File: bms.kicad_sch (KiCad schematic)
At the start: 4 parts, among them U1 BQ76972PFBR

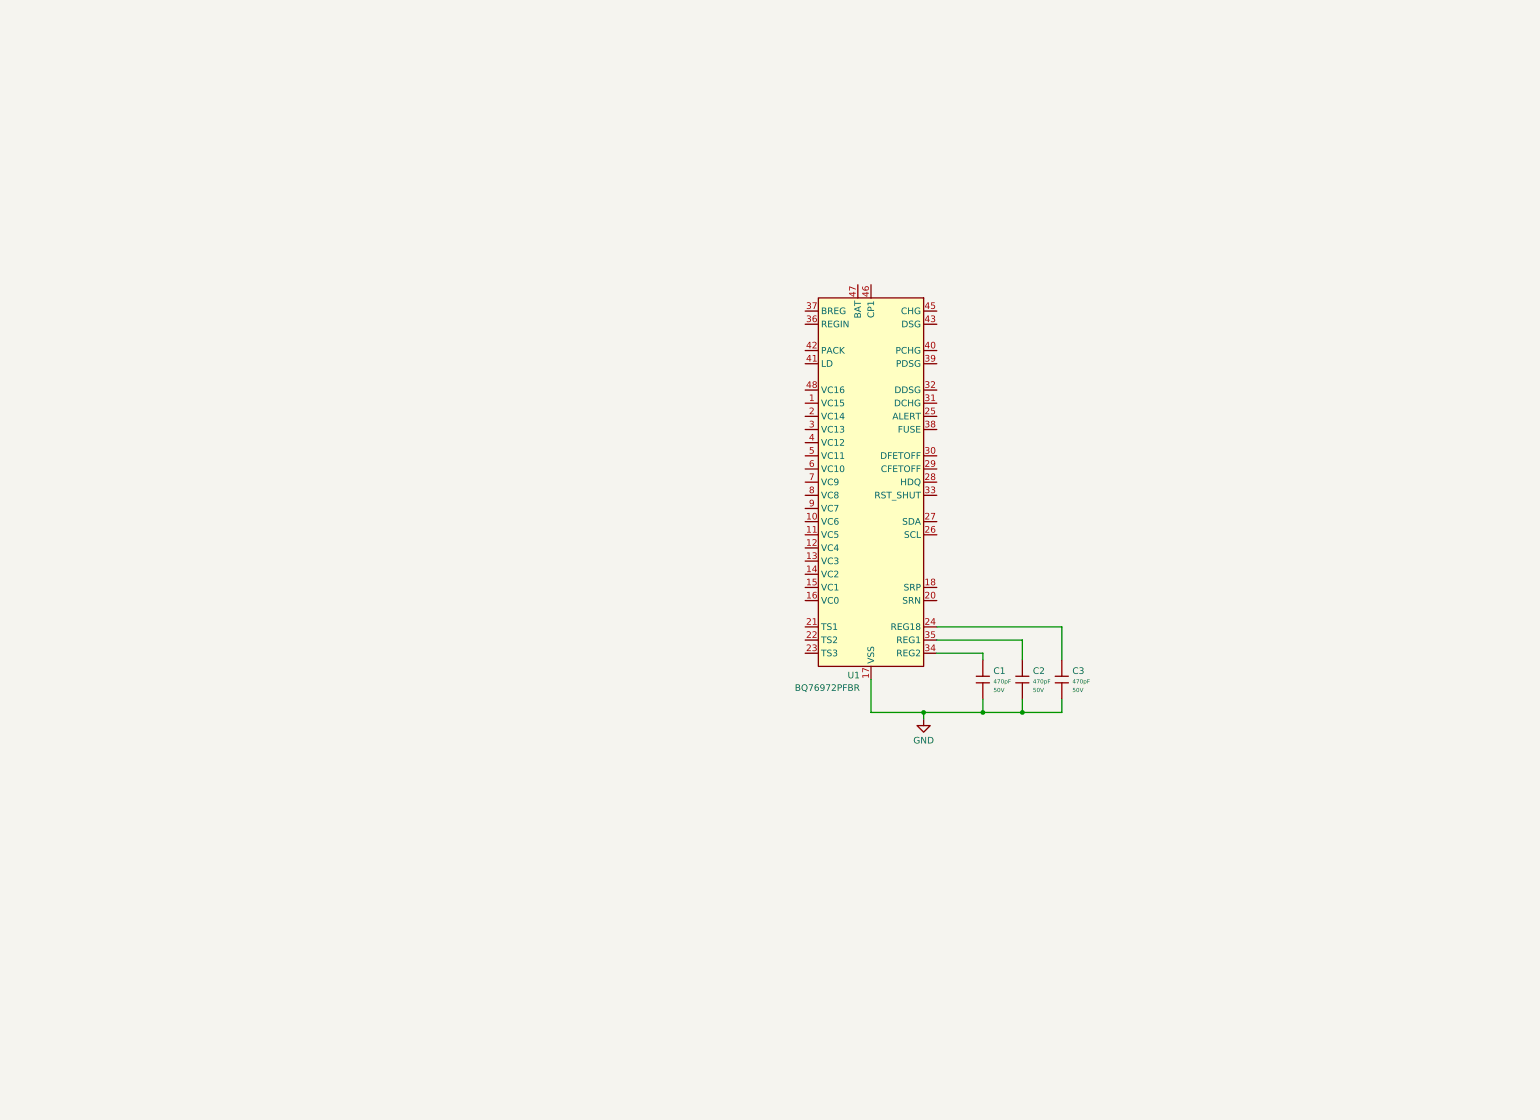
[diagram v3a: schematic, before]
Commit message: removed regulator circuit, more mosfet testing with ltspice
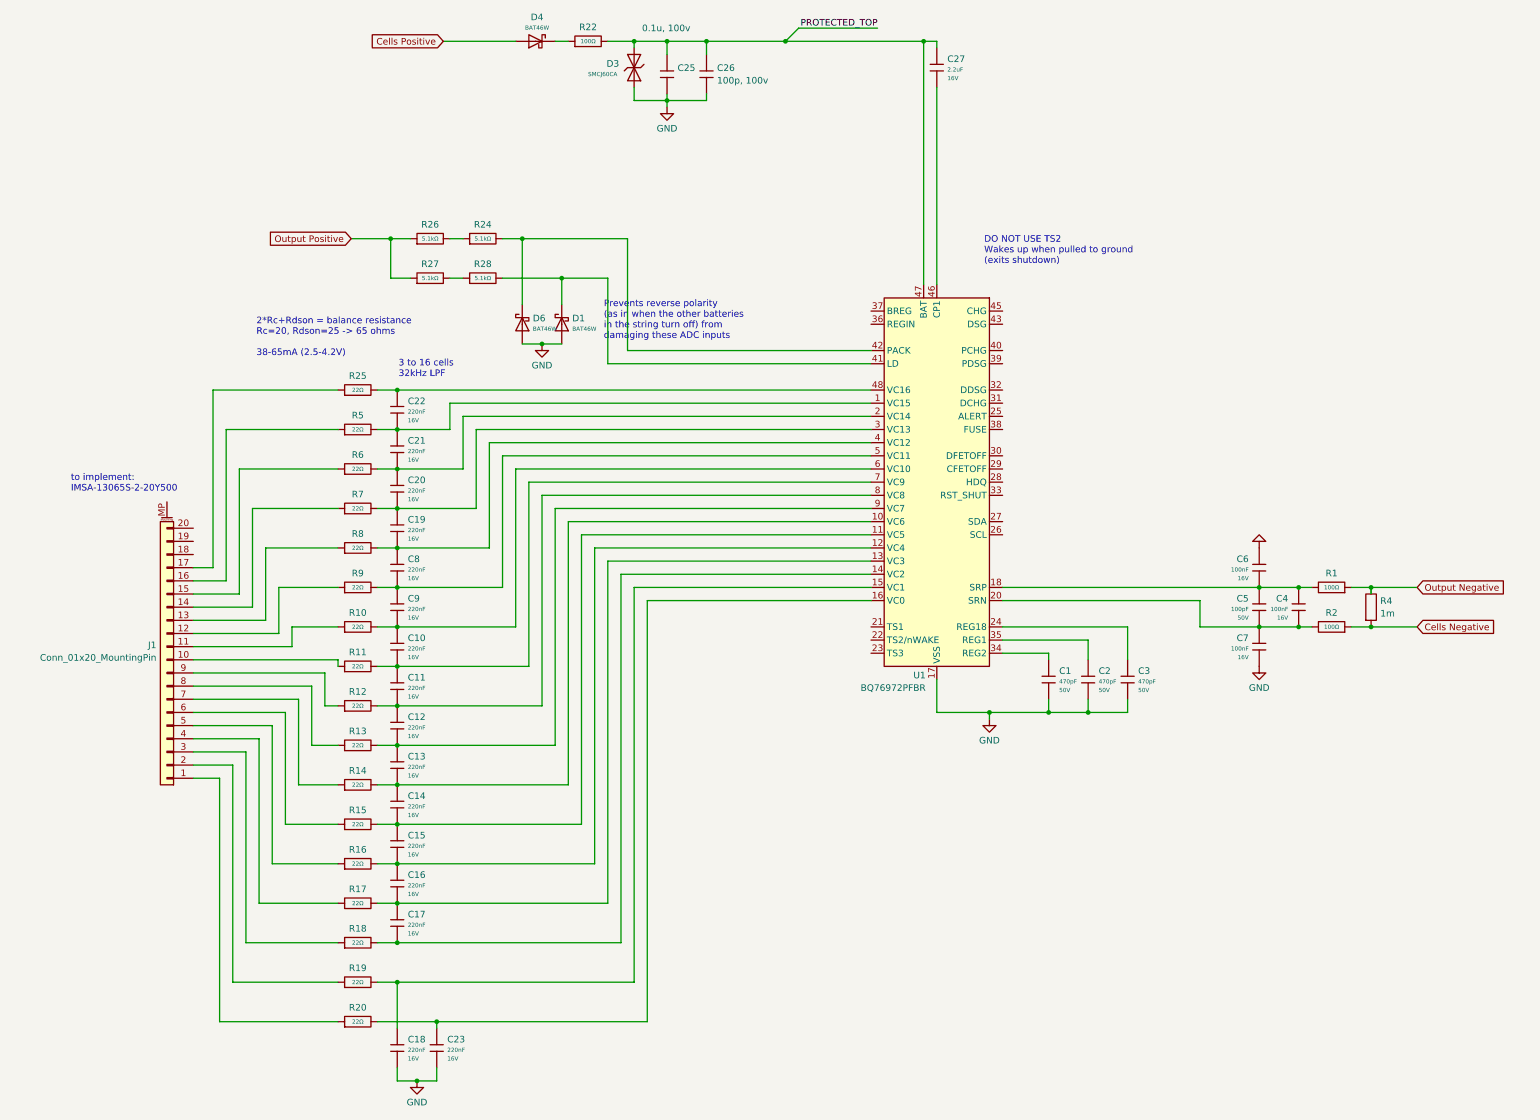
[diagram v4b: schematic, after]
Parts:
- added C10, C11, C12, C13, C14, C15, C16, C17, C18, C19, C20, C21, C22, C23, C8, C9: 220nF, PCM_JLCPCB:C_0402, symbol PCM_JLCPCB-Capacitors:0402,220nF
- added C25: 0.1u, 100v, symbol ct_lib:C
- added C26: 100p, 100v, symbol ct_lib:C
- added C27: 2.2uF, PCM_JLCPCB:C_0603, symbol PCM_JLCPCB-Capacitors:0603,2.2uF
- added C4, C6, C7: 100nF, PCM_JLCPCB:C_0402, symbol PCM_JLCPCB-Capacitors:0402,100nF
- added C5: 100pF, PCM_JLCPCB:C_0402, symbol PCM_JLCPCB-Capacitors:0402,100pF
- added D1, D4, D6: BAT46W, PCM_JLCPCB:D_SOD-123, symbol PCM_JLCPCB-Diodes:Schottky,BAT46W
- added D3: SMCJ60CA, PCM_JLCPCB:D_SMC, symbol PCM_JLCPCB-Diodes:TVS-Bi,SMCJ60CA
- added J1: Conn_01x20_MountingPin, symbol Connector_Generic_MountingPin:Conn_01x20_MountingPin
- added R1, R2, R22: 100Ω, PCM_JLCPCB:R_0402, symbol PCM_JLCPCB-Resistors:0402,100Ω
- added R10, R11, R12, R13, R14, R15, R16, R17, R18, R19, R20, R25, R5, R6, R7, R8, R9: 22Ω, PCM_JLCPCB:R_0402, symbol PCM_JLCPCB-Resistors:0402,22Ω
- added R24, R26, R27, R28: 5.1kΩ, PCM_JLCPCB:R_0402, symbol PCM_JLCPCB-Resistors:0402,5.1kΩ
- added R4: 1m, symbol ct_lib:R
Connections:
- net GND: now also C18.2, C23.2, C25.2, C26.2, C6.1, C7.2, D1.2, D3.1, D6.2
- net at U1.1 (VC15): now also C21.1, C22.2, R5.2
- net at U1.10 (VC6): now also C13.2, C14.1, R14.2
- net at U1.11 (VC5): now also C14.2, C15.1, R15.2
- net at U1.12 (VC4): now also C15.2, C16.1, R16.2
- net at U1.13 (VC3): now also C16.2, C17.1, R17.2
- net at U1.14 (VC2): now also C17.2, R18.2
- net at U1.15 (VC1): now also C18.1, R19.2
- net at U1.16 (VC0): now also C23.1, R20.2
- net at U1.18 (SRP): now also C4.1, C5.1, C6.2, R1.2
- net at U1.2 (VC14): now also C20.1, C21.2, R6.2
- net at U1.20 (SRN): now also C4.2, C5.2, C7.1, R2.2
- net at U1.3 (VC13): now also C19.1, C20.2, R7.2
- net at U1.4 (VC12): now also C19.2, C8.1, R8.2
- net at U1.41 (LD): now also D1.1, R28.2
- net at U1.42 (PACK): now also D6.1, R24.2
- net at U1.46 (CP1): now also C27.2
- net at U1.47 (BAT): now also C25.1, C26.1, C27.1, D3.2, R22.2
- net at U1.48 (VC16): now also C22.1, R25.2
- net at U1.5 (VC11): now also C8.2, C9.1, R9.2
- net at U1.6 (VC10): now also C10.1, C9.2, R10.2
- net at U1.7 (VC9): now also C10.2, C11.1, R11.2
- net at U1.8 (VC8): now also C11.2, C12.1, R12.2
- net at U1.9 (VC7): now also C12.2, C13.1, R13.2
- new net: J1.4 (Pin_4), R17.1
- new net: R27.2, R28.1
- new net: J1.5 (Pin_5), R16.1
- new net: J1.15 (Pin_15), R6.1
- new net: J1.3 (Pin_3), R18.1
- new net: D4.1, R22.1
- new net: J1.17 (Pin_17), R25.1
- new net: J1.14 (Pin_14), R7.1
- new net: J1.12 (Pin_12), R9.1
- new net: R24.1, R26.2
- new net: J1.13 (Pin_13), R8.1
- new net: J1.7 (Pin_7), R14.1
- new net: J1.10 (Pin_10), R11.1
- new net: J1.2 (Pin_2), R19.1
- new net: J1.1 (Pin_1), R20.1
- new net: J1.11 (Pin_11), R10.1
- new net: J1.16 (Pin_16), R5.1
- new net: J1.6 (Pin_6), R15.1
- new net: J1.8 (Pin_8), R13.1
- new net: J1.9 (Pin_9), R12.1
- new net Cells Negative: R2.1, R4.2
- new net Cells Positive: D4.2
- new net Output Negative: R1.1, R4.1
- new net Output Positive: R26.1, R27.1
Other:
- note added: "2*Rc+Rdson = balance resistance Rc=20, Rdson=25 -> 65 ohms 38-65mA (2.5-4.2V)"
- note added: "3 to 16 cells 32kHz LPF"
- note added: "DO NOT USE TS2 Wakes up when pulled to ground (exits shutdown)"
- note added: "Prevents reverse polarity (as in when the other batteries in the string turn off) from damaging these ADC inputs"
- note added: "to implement: IMSA-13065S-2-20Y500"
- moved on the sheet: C1, C2, C3, U1

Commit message: Added new cell balancing circuit to handle 0.4 A at 4V per cell
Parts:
- removed C10, C11, C12, C13, C14, C15, C16, C17, C18, C19, C20, C21, C22, C23, C8, C9: 220nF, PCM_JLCPCB:C_0402, symbol PCM_JLCPCB-Capacitors:0402,220nF
- removed R10, R11, R12, R13, R14, R15, R16, R17, R18, R19, R20, R25, R5, R6, R7, R8, R9: 22Ω, PCM_JLCPCB:R_0402, symbol PCM_JLCPCB-Resistors:0402,22Ω
- added C10, C11, C12, C13, C14, C15, C16, C17, C18, C19, C20, C21, C22, C23, C24, C8, C9: 220nF, PCM_JLCPCB:C_0805, symbol PCM_JLCPCB-Capacitors:0805,220nF
- added D1: BZT52C3V6, PCM_JLCPCB:D_SOD-123, symbol PCM_JLCPCB-Diodes:Zener,BZT52C3V6
- added D2, D6: BAT46W, PCM_JLCPCB:D_SOD-123, symbol PCM_JLCPCB-Diodes:Schottky,BAT46W
- added Q1, Q10, Q11, Q12, Q13, Q14, Q15, Q16, Q2, Q3, Q4, Q5, Q6, Q7, Q8, Q9: PBSS4350T,215, Package_TO_SOT_SMD:SOT-23, symbol ct_lib:PBSS4350T,215
- added R10, R12, R15, R18, R21, R29, R3, R32, R35, R38, R41, R44, R47, R5, R50, R53, R56: 330Ω, PCM_JLCPCB:R_0402, symbol PCM_JLCPCB-Resistors:0402,330Ω
- added R11, R13, R16, R19, R23, R30, R33, R36, R39, R42, R45, R48, R51, R54, R57, R6: 82R, PCM_JLCPCB:R_0402, symbol ct_lib:FRC0402J820_TS
- added R14, R17, R20, R25, R31, R34, R37, R40, R43, R46, R49, R52, R55, R7, R8, R9: 10R, Resistor_SMD:R_2512_6332Metric, symbol ct_lib:FRP2512J100 TS
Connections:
- net GND: now also U1.36 (REGIN), U1.37 (BREG), C8.2, C9.2, D1.2, D6.2
- net Cell3: now reaches J1.4 (Pin_4)
- net Cell3: now also Q4.2 (E), R12.1, R9.2
- net VC3: now reaches U1.13 (VC3)
- net VC3: now also C11.1, C12.2, R12.2, R16.2
- net VC14: now reaches U1.2 (VC14)
- net VC14: now also C22.1, C23.2, R50.2, R54.2
- net VC13: now reaches U1.3 (VC13)
- net VC13: now also C21.1, C22.2, R47.2, R51.2
- net Cell4: now reaches J1.5 (Pin_5)
- net Cell4: now also Q5.2 (E), R14.2, R15.1
- net VC4: now reaches U1.12 (VC4)
- net VC4: now also C12.1, C13.2, R15.2, R19.2
- net Cell14: now reaches J1.15 (Pin_15)
- net Cell14: now also Q15.2 (E), R49.2, R50.1
- net Cell2: now reaches J1.3 (Pin_3)
- net Cell2: now also Q3.2 (E), R5.1, R8.2
- net VC2: now reaches U1.14 (VC2)
- net VC2: now also C10.1, C11.2, R13.2, R5.2
- net VC8: now reaches U1.8 (VC8)
- net VC8: now also C16.1, C17.2, R32.2, R36.2
- net VC7: now reaches U1.9 (VC7)
- net VC7: now also C15.1, C16.2, R29.2, R33.2
- net Cell16: now reaches J1.17 (Pin_17)
- net Cell16: now also R55.2, R56.1
- net VC16: now reaches U1.48 (VC16)
- net VC16: now also C24.1, D2.1, R56.2
- net VC6: now reaches U1.10 (VC6)
- net VC6: now also C14.1, C15.2, R21.2, R30.2
- net Cell13: now reaches J1.14 (Pin_14)
- net Cell13: now also Q14.2 (E), R46.2, R47.1
- net VC1: now reaches U1.15 (VC1)
- net VC1: now also C10.2, C8.1, R3.2, R6.2
- net VC5: now reaches U1.11 (VC5)
- net VC5: now also C13.1, C14.2, R18.2, R23.2
- net VC0: now reaches U1.16 (VC0)
- net VC0: now also C9.1, D1.1, D6.1, R10.2, R11.2
- net VC15: now reaches U1.1 (VC15)
- net VC15: now also C23.1, C24.2, D2.2, R53.2, R57.2
- net Cell11: now reaches J1.12 (Pin_12)
- net Cell11: now also Q12.2 (E), R40.2, R41.1
- net VC11: now reaches U1.5 (VC11)
- net VC11: now also C19.1, C20.2, R41.2, R45.2
- net VC10: now reaches U1.6 (VC10)
- net VC10: now also C18.1, C19.2, R38.2, R42.2
- net VC9: now reaches U1.7 (VC9)
- net VC9: now also C17.1, C18.2, R35.2, R39.2
- net VC12: now reaches U1.4 (VC12)
- net VC12: now also C20.1, C21.2, R44.2, R48.2
- net Cell12: now reaches J1.13 (Pin_13)
- net Cell12: now also Q13.2 (E), R43.2, R44.1
- net Cell6: now reaches J1.7 (Pin_7)
- net Cell6: now also Q7.2 (E), R20.2, R21.1
- net Cell9: now reaches J1.10 (Pin_10)
- net Cell9: now also Q10.2 (E), R34.2, R35.1
- net Cell1: now reaches J1.2 (Pin_2)
- net Cell1: now also Q2.2 (E), R3.1, R7.2
- net Cell0: now reaches J1.1 (Pin_1)
- net Cell0: now also Q1.2 (E), R10.1
- net Cell10: now reaches J1.11 (Pin_11)
- net Cell10: now also Q11.2 (E), R37.2, R38.1
- net Cell15: now reaches J1.16 (Pin_16)
- net Cell15: now also Q16.2 (E), R52.2, R53.1
- net Cell5: now reaches J1.6 (Pin_6)
- net Cell5: now also Q6.2 (E), R17.2, R18.1
- net Cell7: now reaches J1.8 (Pin_8)
- net Cell7: now also Q8.2 (E), R25.2, R29.1
- net Cell8: now reaches J1.9 (Pin_9)
- net Cell8: now also Q9.2 (E), R31.2, R32.1
- new net: Q7.3 (C), R25.1
- new net: Q16.3 (C), R55.1
- new net: Q12.3 (C), R43.1
- new net: Q6.3 (C), R20.1
- new net: Q10.3 (C), R37.1
- new net: Q14.1 (B), R51.1
- new net: Q14.3 (C), R49.1
- new net: Q1.3 (C), R7.1
- new net: Q13.3 (C), R46.1
- new net: Q6.1 (B), R23.1
- new net: Q2.1 (B), R6.1
- new net: Q2.3 (C), R8.1
- new net: Q15.1 (B), R54.1
- new net: Q15.3 (C), R52.1
- new net: Q10.1 (B), R39.1
- new net: Q11.3 (C), R40.1
- new net: Q5.1 (B), R19.1
- new net: Q5.3 (C), R17.1
- new net: Q13.1 (B), R48.1
- new net: Q3.1 (B), R13.1
- new net: Q9.1 (B), R36.1
- new net: Q9.3 (C), R34.1
- new net: Q12.1 (B), R45.1
- new net: Q16.1 (B), R57.1
- new net: Q8.3 (C), R31.1
- new net: Q1.1 (B), R11.1
- new net: Q11.1 (B), R42.1
- new net: Q4.1 (B), R16.1
- new net: Q8.1 (B), R33.1
- new net: Q3.3 (C), R9.1
- new net: Q4.3 (C), R14.1
- new net: Q7.1 (B), R30.1
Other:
- note added: "NPN: 13mA IB 420mA IC ~100mW at 0.2VCE Possible: ZXTN4240F-7 PBSS4350T,215"
- note added: "re-evaluate. these bitches are exploding at 450V reverse (20W) might just need a dumb fuse. FETs will probably cut in time to save these from exploding anyways. Fuse to guarantee fail-open"
- note removed: "2*Rc+Rdson = balance resistance Rc=20, Rdson=25 -> 65 ohms 38-65mA (2.5-4.2V)"
- note removed: "3 to 16 cells 32kHz LPF"
- moved on the sheet: C1, C2, C25, C26, C27, C3, C4, C5, C6, C7, D1, D3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

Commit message: Updated simulations to fix turn-off issues at negative voltages. Added power stage to BMS based on sim 5
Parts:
- removed D1: BZT52C3V6, PCM_JLCPCB:D_SOD-123, symbol PCM_JLCPCB-Diodes:Zener,BZT52C3V6
- removed D3: SMCJ60CA, PCM_JLCPCB:D_SMC, symbol PCM_JLCPCB-Diodes:TVS-Bi,SMCJ60CA
- removed D6 (x2): BAT46W, PCM_JLCPCB:D_SOD-123, symbol PCM_JLCPCB-Diodes:Schottky,BAT46W
- removed R24, R26, R27, R28: 5.1kΩ, PCM_JLCPCB:R_0402, symbol PCM_JLCPCB-Resistors:0402,5.1kΩ
- added C1, C2, C3, C4, C5, C6, C7, C8: 470pF, PCM_JLCPCB:C_0402, symbol PCM_JLCPCB-Capacitors:0402,470pF
- added D2: BZT52C3V6, PCM_JLCPCB:D_SOD-123, symbol PCM_JLCPCB-Diodes:Zener,BZT52C3V6
- added D3: SMCJ64CA, PCM_JLCPCB:D_SMC, symbol PCM_JLCPCB-Diodes:TVS-Bi,SMCJ64CA
- added D4, D?: BZT52C75, PCM_JLCPCB:D_SOD-123, symbol PCM_JLCPCB-Diodes:Zener,BZT52C75
- added D5, D?: BAT46W, PCM_JLCPCB:D_SOD-123, symbol PCM_JLCPCB-Diodes:Schottky,BAT46W
- added D6: Red, PCM_JLCPCB:D_0603, symbol PCM_JLCPCB-Diodes:LED,0603,Red
- added J1: Conn_01x10, symbol Connector_Generic:Conn_01x10
- added Q1, Q2: DMZ6012E, Package_TO_SOT_SMD:TSOT-23, symbol ct_lib:DMZ6012E
- added Q5: BSS123, PCM_JLCPCB:Q_SOT-23, symbol PCM_JLCPCB-Transistors:NMOS,BSS123
- added R1, R2, R3, R8: 5.1kΩ, PCM_JLCPCB:R_0402, symbol PCM_JLCPCB-Resistors:0402,5.1kΩ
- added R10, R9: 7.5kΩ, PCM_JLCPCB:R_0402, symbol PCM_JLCPCB-Resistors:0402,7.5kΩ
- added R11: 10kΩ, PCM_JLCPCB:R_0402, symbol PCM_JLCPCB-Resistors:0402,10kΩ
- added R12: 100kΩ, PCM_JLCPCB:R_0402, symbol PCM_JLCPCB-Resistors:0402,100kΩ
- added R13: 18kR, PCM_JLCPCB:R_0402, symbol ct_lib:RT0402BRD0718KL
- added TH1, TH2: 10k, PCM_JLCPCB:R_0402, symbol ct_lib:B57232V5103F360
- C?: renamed from C25; value 0.1u, 100v -> 2.2u, 100v
- renumbered C16 to C?, C24 to C?, C20 to C?, C1 to C?, C27 to C?, C10 to C?, C22 to C?, C14 to C?, C19 to C?, C3 to C?, C17 to C?, C9 to C?, C2 to C?, C26 to C?, C21 to C?, C23 to C?, C8 to C?, C12 to C?, C18 to C?, C7 to C?, C15 to C?, C11 to C?, C13 to C?, C6 to C?, C5 to C?, C4 to C?, D4 to D?, D2 to D?, J1 to J?, Q14 to Q?, Q2 to Q?, Q15 to Q?, Q6 to Q?, Q10 to Q?, Q5 to Q?, Q13 to Q?, Q12 to Q?, Q1 to Q?, Q3 to Q?, Q11 to Q?, Q9 to Q?, Q16 to Q?, Q4 to Q?, Q7 to Q?, Q8 to Q?, R25 to R?, R55 to R?, R43 to R?, R20 to R?, R37 to R?, R10 to R?, R7 to R?, R53 to R?, R38 to R?, R46 to R?, R22 to R?, R23 to R?, R40 to R?, R21 to R?, R17 to R?, R39 to R?, R35 to R?, R13 to R?, R41 to R?, R50 to R?, R36 to R?, R19 to R?, R32 to R?, R34 to R?, R15 to R?, R45 to R?, R57 to R?, R31 to R?, R44 to R?, R29 to R?, R4 to R?, R1 to R?, R51 to R?, R6 to R?, R42 to R?, R56 to R?, R16 to R?, R12 to R?, R47 to R?, R33 to R?, R18 to R?, R5 to R?, R11 to R?, R14 to R?, R54 to R?, R9 to R?, R30 to R?, R52 to R?, R49 to R?, R2 to R?, R3 to R?, R48 to R?, R8 to R?, U1 to U?
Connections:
- net Cells Positive: now also R10.1; no longer D?.2
- net GND: now also C1.2, C2.2, C3.2, C4.2, C5.2, C6.2, C7.2, C8.2, D2.2, D3.1, D4.2, D5.2, D?.2, D?.2, J1.10 (Pin_10), J1.2 (Pin_2), J1.4 (Pin_4), J1.6 (Pin_6), J1.8 (Pin_8), Q5.2 (S), R12.2, R13.2, TH1.1, TH2.1
- net VC0: now also D1.1, D2.1
- net LD: now reaches U?.41 (LD)
- net LD: now also D4.1, D?.1, Q2.3 (D); no longer D1.1
- net at C?.1, C?.1, C?.1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: now also D3.2
- net CHARGE_PUMP: now reaches C?.2, U?.46 (CP1)
- net TEMP1: now reaches U?.21 (TS1)
- net TEMP1: now also C1.1, J1.1 (Pin_1)
- net TEMP2: now reaches U?.23 (TS3)
- net TEMP2: now also C2.1, J1.3 (Pin_3)
- net TEMP5: now reaches U?.25 (ALERT)
- net TEMP5: now also C5.1, J1.9 (Pin_9)
- net AFE_SDL: now reaches U?.26 (SCL)
- net AFE_SDA: now reaches U?.27 (SDA)
- net TEMP_CAL: now reaches U?.28 (HDQ)
- net TEMP_CAL: now also C8.1, R13.1
- net TEMP_CHG: now reaches U?.29 (CFETOFF)
- net TEMP_CHG: now also C7.1, TH1.2
- net TEMP_DSG: now reaches U?.30 (DFETOFF)
- net TEMP_DSG: now also C6.1, TH2.2
- net TEMP4: now reaches U?.31 (DCHG)
- net TEMP4: now also C4.1, J1.7 (Pin_7)
- net TEMP3: now reaches U?.32 (DDSG)
- net TEMP3: now also C3.1, J1.5 (Pin_5)
- net Fuse: now reaches U?.38 (FUSE)
- net Fuse: now also R11.2
- net PACK: now reaches U?.42 (PACK)
- net PACK: now also D5.1, D?.1, Q1.3 (D)
- net DSG_GATE_CTRL: now reaches U?.43 (DSG)
- net CHG_GATE_CTRL: now reaches U?.45 (CHG)
- net Cells Negative renamed CELLS_NEGATIVE
- net Output Negative renamed OUTPUT_NEGATIVE
- new net: R10.2, R9.1
- new net: D6.2, R9.2
- new net: Q1.2 (S), R3.2
- new net: Q5.1 (G), R11.1, R12.1
- new net: D6.1, Q5.3 (D)
- new net: R3.1, R8.2
- new net: Q2.2 (S), R2.2
- new net: R1.2, R2.1
- new net CELLS_POSITIVE: D?.2
- new net OUTPUT_POSITIVE: Q1.1 (G), Q2.1 (G), R1.1, R8.1
- no-connect marks 0 -> 1
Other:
- note added: "2x 0402 for >72V creepage"
- note added: "Balancing"
- note added: "Cell Header"
- note added: "Current Sense"
- note added: "Diagram: Balance current"
- note added: "Diodes protect analog I/O against -450V reverse polarity Depletion NMOS protects against over-powering 5.1k resistors (-450V expected when this battery turns off first in the string)"
- note added: "Fault LED"
- note added: "LD will not let pack recover until load is >30k across output terminals (LD must rise >4V with 100uA excitation)"
- note added: "Prevents ground straying too far during short circuits"
- note added: "Terminal Analog Pins"
- note added: "Thermistors"
- note added: "VC0: VSS-0.3 to VSS+6 Else: VSS-0.3 to VSS+85"
- note removed: "Prevents reverse polarity (as in when the other batteries in the string turn off) from damaging these ADC inputs"
- note removed: "re-evaluate. these bitches are exploding at 450V reverse (20W) might just need a dumb fuse. FETs will probably cut in time to save these from exploding anyways. Fuse to guarantee fail-open"
- moved on the sheet: C?, D?, J?, Q?, R?, U?
